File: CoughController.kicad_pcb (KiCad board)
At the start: 2 copper layers, 99 x 85 mm, 50 parts, among them J3 AUDIO IN/OUT, J4 DIO-2, J5 GPIO-OUT, J6 GPIO-IN, K1 G6A-274P-ST-US DC12, K2 G6A-274P-ST-US DC12, U1 TLP627-2, U2 TLP627-2, U3 TLP627-2, U4 TLP627-2, U5 TLP627-2, U6 TLP627-2

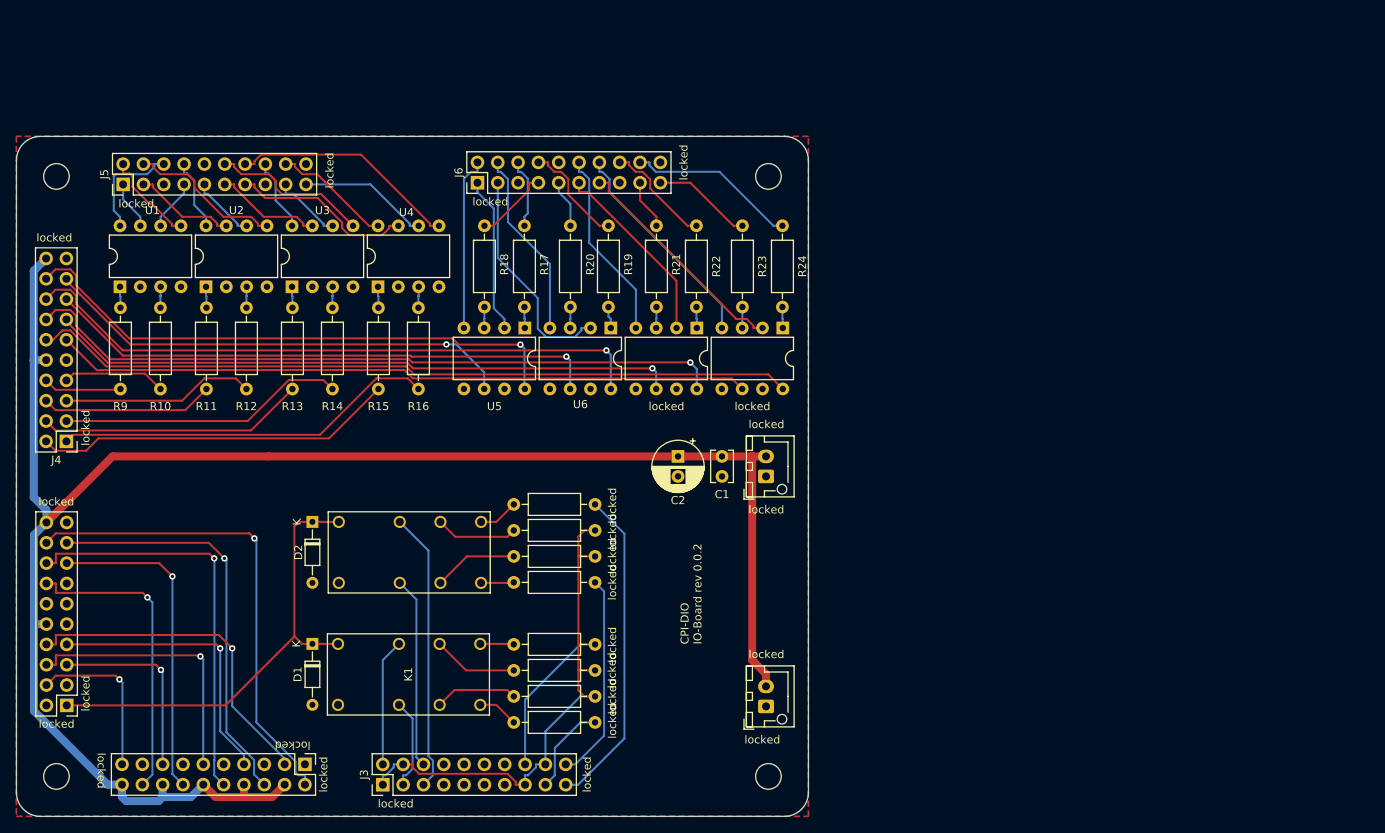
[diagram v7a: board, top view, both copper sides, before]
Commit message: GPIO OUT ジックミスを修正
電流シンクに変更
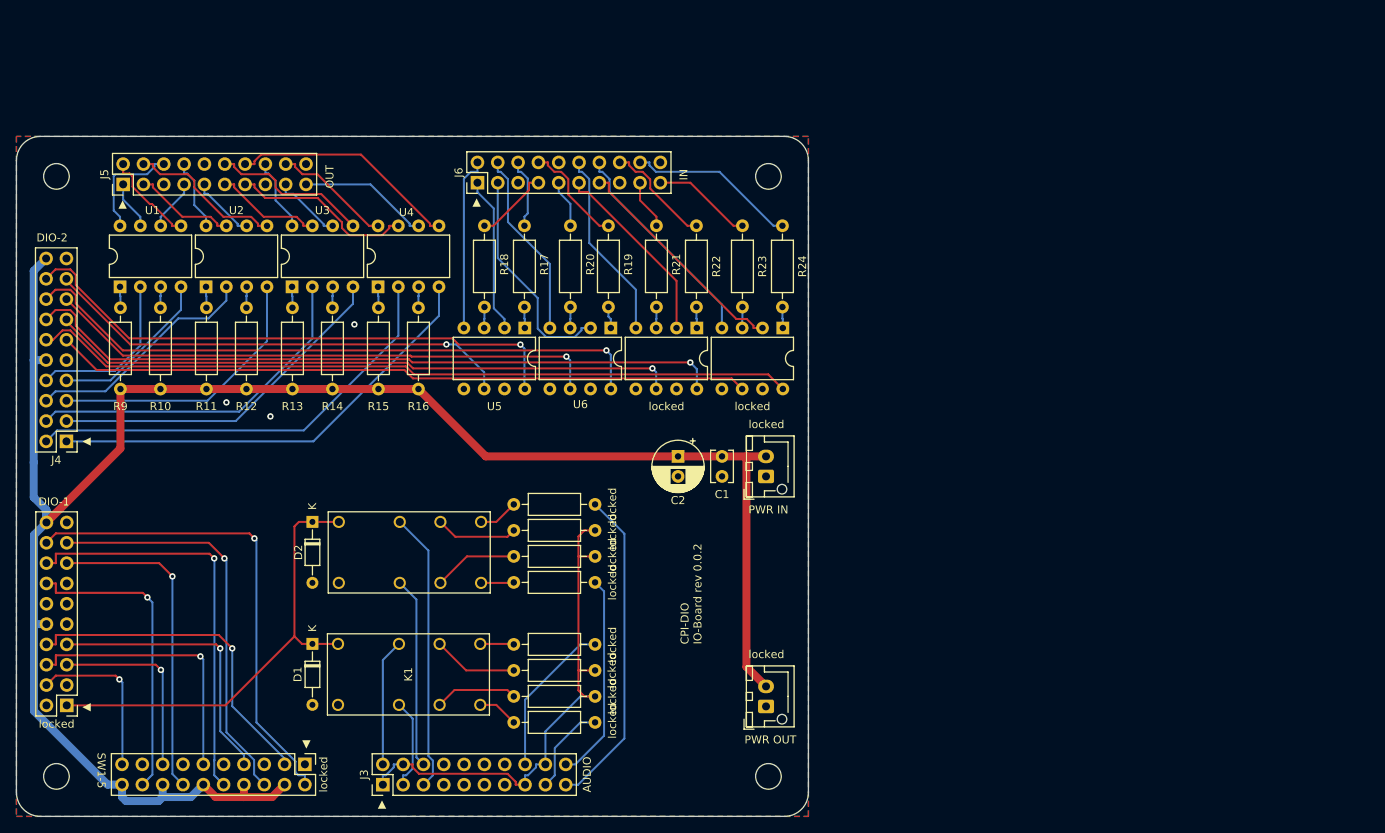
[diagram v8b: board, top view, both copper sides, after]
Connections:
- R10 pad 2: DIO-2/OUT2 -> COM0
- R11 pad 2: DIO-2/OUT3 -> COM0
- R12 pad 2: DIO-2/OUT4 -> COM0
- R13 pad 2: DIO-2/OUT5 -> COM0
- R14 pad 2: DIO-2/OUT6 -> COM0
- R15 pad 2: DIO-2/OUT7 -> COM0
- R16 pad 2: DIO-2/OUT8 -> COM0
- R9 pad 2: DIO-2/OUT1 -> COM0
- U1 pad 2: MCOM1 -> DIO-2/OUT1
- U1 pad 4: MCOM1 -> DIO-2/OUT2
- U2 pad 2: MCOM1 -> DIO-2/OUT3
- U2 pad 4: MCOM1 -> DIO-2/OUT4
- U3 pad 2: MCOM1 -> DIO-2/OUT5
- U3 pad 4: MCOM1 -> DIO-2/OUT6
- U4 pad 2: MCOM1 -> DIO-2/OUT7
- U4 pad 4: MCOM1 -> DIO-2/OUT8
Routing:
- net COM0: track 226.6 -> 239.7 mm
- net DIO-2/OUT1: track 9.82 -> 20.9 mm
- net DIO-2/OUT4: track 24.2 -> 35.0 mm
- net DIO-2/OUT5: track 33.4 -> 44.0 mm
- net DIO-2/OUT7: track 45.2 -> 55.6 mm
- net DIO-2/OUT8: track 47.8 -> 56.7 mm
- net DIO-2/OUT6: track 35.8 -> 44.0 mm
- net DIO-2/OUT2: track 12.9 -> 20.9 mm
- net DIO-2/OUT3: track 21.6 -> 29.4 mm
- net MCOM1: vias 0 -> 3
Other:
- board text added: "AUDIO"
- board text added: "DIO-1"
- board text added: "DIO-2"
- board text added: "IN"
- board text added: "OUT"
- board text added: "PWR IN"
- board text added: "PWR OUT"
- board text added: "SW1-5"
- board text added: "▲"
- board text removed: "locked"
